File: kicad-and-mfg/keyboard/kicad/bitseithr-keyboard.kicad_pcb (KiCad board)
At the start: 2 copper layers, 365 x 206 mm, 103 parts, among them P2 KEYB CONN 1

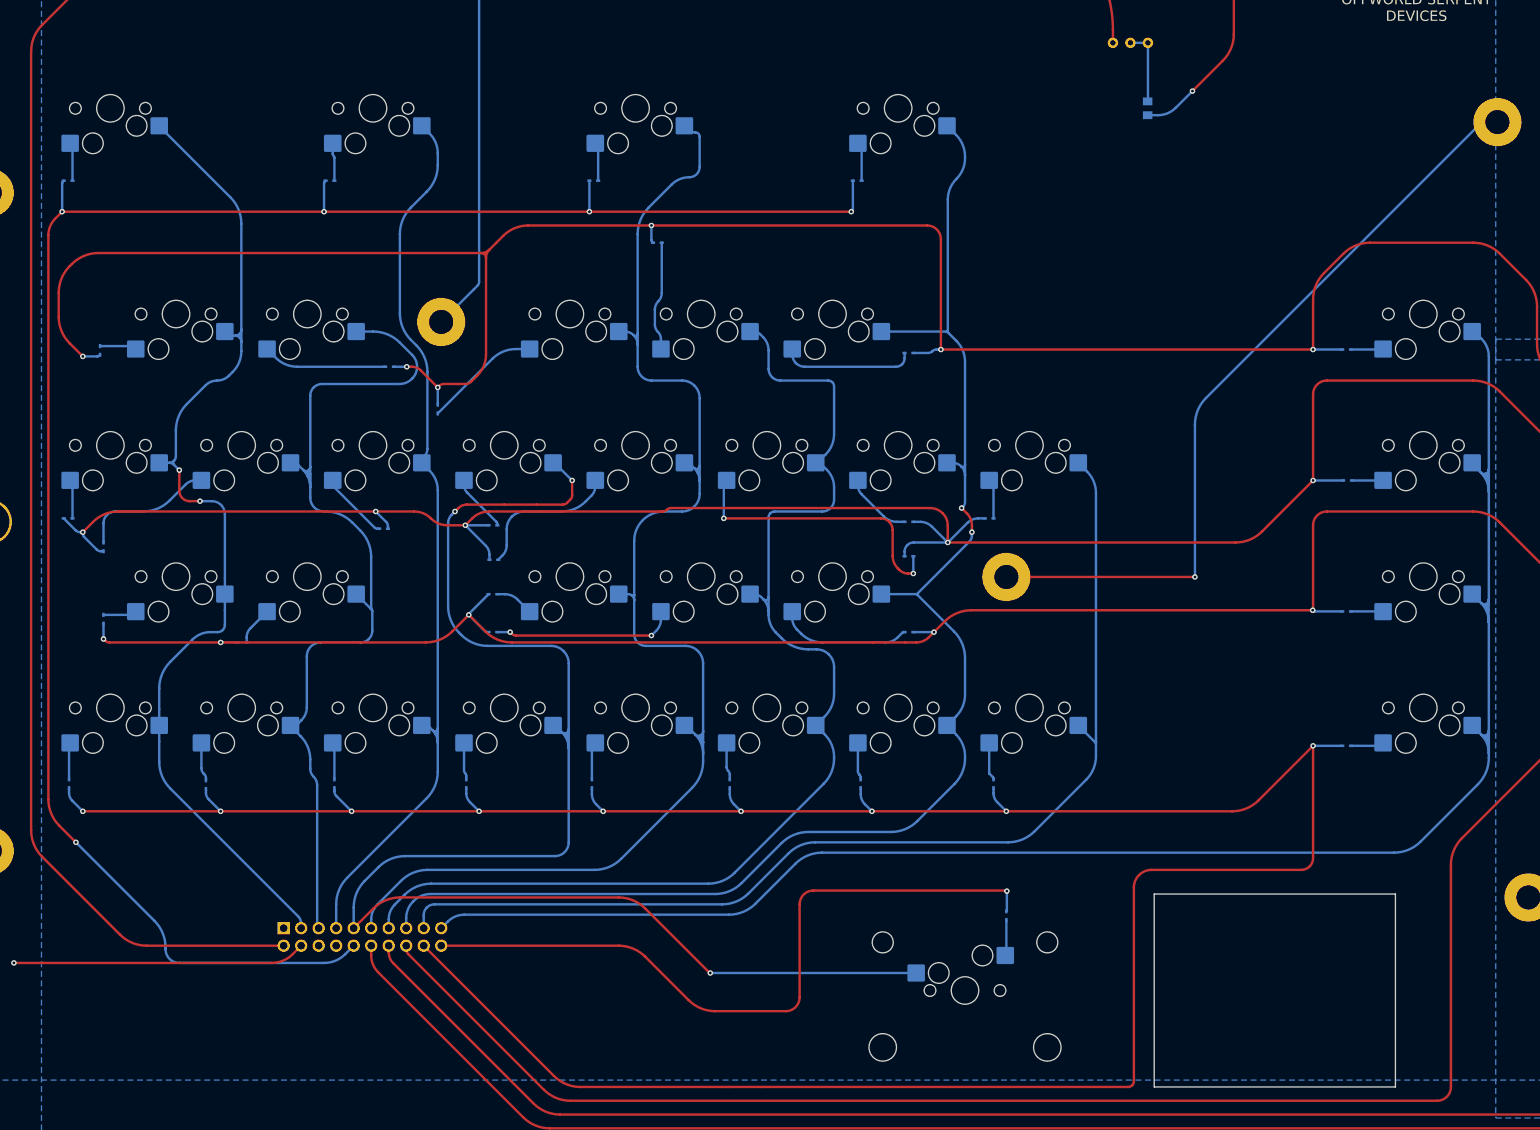
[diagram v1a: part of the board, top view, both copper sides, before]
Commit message: fixed drc from kicad 10 upgrade, but origin has shifted 1.5 mm left (means board coords are +1.5mm)
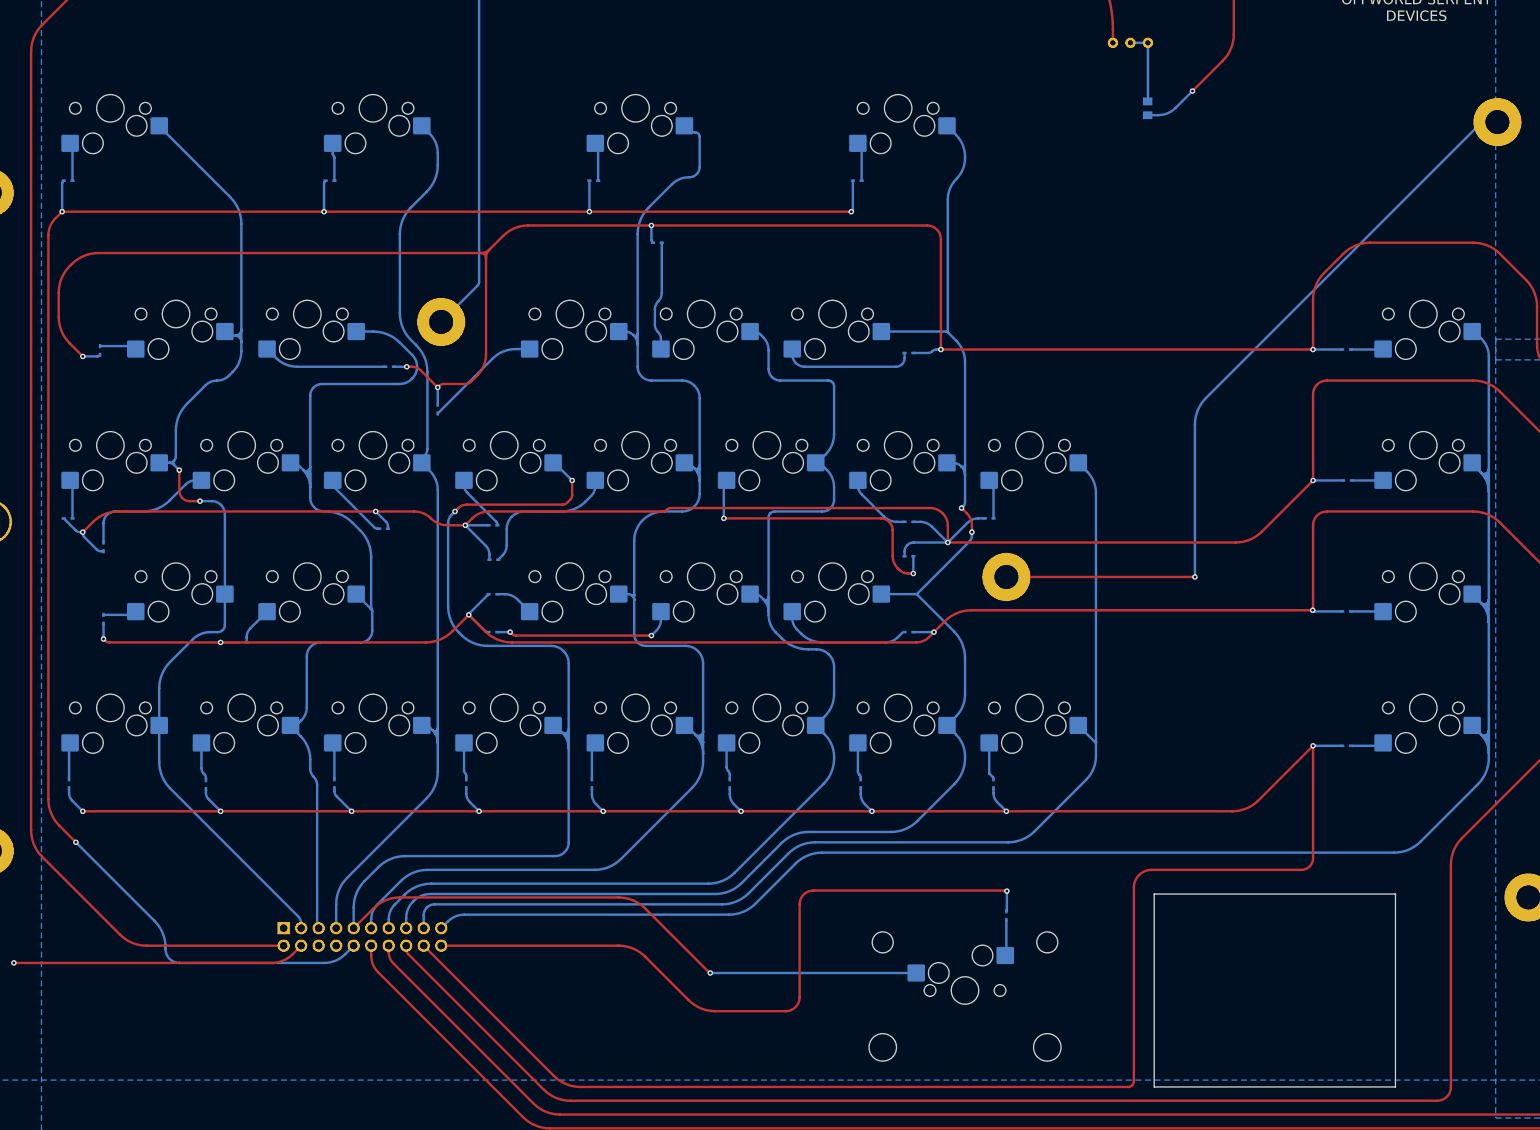
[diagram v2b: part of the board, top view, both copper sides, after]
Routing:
- net GND: track 215.9 -> 212.6 mm
- net COL4: track 201.7 -> 198.8 mm
- net COL1: track 134.2 -> 131.8 mm
- net COL0: track 152.3 -> 150.3 mm
- net COL2: track 131.8 -> 129.9 mm
- net Net-(D29-A): track 19.4 -> 18.1 mm
- net Net-(D31-A): track 5.73 -> 4.45 mm
- net Net-(D12-A): track 10.0 -> 8.91 mm
- net Net-(D26-A): track 5.60 -> 4.49 mm
- net Net-(D21-A): track 5.45 -> 4.44 mm
- net Net-(D5-A): track 4.84 -> 3.88 mm
- net Net-(D3-A): track 5.33 -> 4.45 mm
- net COL5: track 170.9 -> 170.0 mm
- net Net-(D36-A): track 4.80 -> 3.94 mm
- net Net-(D8-A): track 19.5 -> 18.6 mm
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
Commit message: moved keyboard pcb 1.5mm left, started shield schematic
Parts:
- moved D10 1.50 mm to (75.9, 196.1)
- moved D11 1.50 mm to (93.9, 108.5)
- moved D12 1.50 mm to (101.6, 159.0)
- moved D13 1.50 mm to (94.5, 196.0)
- moved D14 1.50 mm to (117.5, 158.5)
- moved D15 1.50 mm to (113.6, 196.0)
- moved D16 1.50 mm to (192.0, 215.1)
- moved D17 1.50 mm to (132.1, 108.5)
- moved D18 1.50 mm to (109.5, 141.6)
- moved D19 1.50 mm to (117.6, 163.5)
- moved D2 1.50 mm to (55.9, 108.5)
- moved D20 1.50 mm to (117.5, 168.5)
- moved D21 1.50 mm to (131.9, 196.0)
- moved D22 1.50 mm to (141.4, 117.5)
- moved D23 1.50 mm to (177.9, 163.0)
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
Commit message: made one tiny re-route, fixed drc warnings from that
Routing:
- net +9V: track 373.4 -> 364.0 mm
- net COL8: track 252.0 -> 255.6 mm
- net COL4: track 198.8 -> 200.0 mm
